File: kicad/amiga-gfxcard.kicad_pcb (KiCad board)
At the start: 2 copper layers, 127 x 59.1 mm, 34 parts, among them P1 ADDR1, P10 AUX1B, P11 AUX2A, P12 AUX2B, P2 ADDR2, P3 ADDR4, P4 DATA2, P5 ADDR3, P6 DATA1, P7 CTRL_OUT, P8 CONN_01X02, P9 AUX1A, U1 74LVC8T245, U2 74LVC8T245, U3 74LVC8T245, U4 74LVC8T245, U5 74LVC8T245, U6 74LVC8T245

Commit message: board v1.2 finished
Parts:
- removed P10: AUX1B, Pin_Headers:Pin_Header_Straight_1x08
- removed P11: AUX2A, Pin_Headers:Pin_Header_Straight_1x04
- removed P12: AUX2B, Pin_Headers:Pin_Header_Straight_1x04
- removed P7: CTRL_OUT, Pin_Headers:Pin_Header_Straight_1x04
- removed P9: AUX1A, Pin_Headers:Pin_Header_Straight_1x08
- added G***: LOGO, mnt:mnt, F.Cu at (203.2, 49.7)
- added P13: X1, Pin_Headers:Pin_Header_Straight_1x08, F.Cu at (137.8, 50.2)
- added P14: X2, Pin_Headers:Pin_Header_Straight_1x08, F.Cu at (137.8, 47.6)
- added P16: D1, Pin_Headers:Pin_Header_Straight_1x03, F.Cu at (130.3, 94.6)
- moved C1 45.7 mm to (102.5, 104.0)
- moved C10 45.7 mm to (121.4, 113.0)
- moved C11 45.7 mm to (142.2, 103.9)
- moved C12 45.7 mm to (184.2, 114.2)
- moved C2 45.7 mm to (162.0, 113.0)
- moved C3 45.7 mm to (152.1, 103.9)
- moved C4 45.7 mm to (102.5, 113.0)
- moved C5 45.7 mm to (161.9, 103.9)
- moved C6 45.7 mm to (152.1, 112.8)
- moved C7 45.7 mm to (184.2, 104.0)
- moved C8 45.7 mm to (142.2, 112.8)
- moved C9 45.7 mm to (121.4, 104.0)
- moved P1 45.7 mm to (137.9, 92.1)
- moved P2 45.7 mm to (137.9, 94.6)
- moved P3 45.7 mm to (158.2, 94.6)
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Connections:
- CON-Z21 pad 10: Net-(CON-Z21-Pad10) -> (no net)
- CON-Z21 pad 14: Net-(CON-Z21-Pad14) -> (no net)
- CON-Z21 pad 15: Net-(CON-Z21-Pad15) -> (no net)
- CON-Z21 pad 16: Net-(CON-Z21-Pad16) -> (no net)
- CON-Z21 pad 17: Net-(CON-Z21-Pad17) -> (no net)
- CON-Z21 pad 18: Net-(CON-Z21-Pad18) -> (no net)
- CON-Z21 pad 19: Net-(CON-Z21-Pad19) -> (no net)
- CON-Z21 pad 20: Net-(CON-Z21-Pad20) -> (no net)
- CON-Z21 pad 22: Net-(CON-Z21-Pad22) -> (no net)
- CON-Z21 pad 31: Net-(CON-Z21-Pad31) -> (no net)
- CON-Z21 pad 33: Net-(CON-Z21-Pad33) -> (no net)
- CON-Z21 pad 35: Net-(CON-Z21-Pad35) -> (no net)
- CON-Z21 pad 40: Net-(CON-Z21-Pad40) -> (no net)
- CON-Z21 pad 42: Net-(CON-Z21-Pad42) -> (no net)
- CON-Z21 pad 44: Net-(CON-Z21-Pad44) -> (no net)
- CON-Z21 pad 48: Net-(CON-Z21-Pad48) -> (no net)
- CON-Z21 pad 50: Net-(CON-Z21-Pad50) -> (no net)
- CON-Z21 pad 51: Net-(CON-Z21-Pad51) -> (no net)
- CON-Z21 pad 55: Net-(CON-Z21-Pad55) -> (no net)
- CON-Z21 pad 60: Net-(CON-Z21-Pad60) -> (no net)
- CON-Z21 pad 62: Net-(CON-Z21-Pad62) -> (no net)
- CON-Z21 pad 64: Net-(CON-Z21-Pad64) -> (no net)
- CON-Z21 pad 66: Net-(CON-Z21-Pad66) -> (no net)
- CON-Z21 pad 7: Net-(CON-Z21-Pad7) -> (no net)
- CON-Z21 pad 8: Net-(CON-Z21-Pad8) -> (no net)
- CON-Z21 pad 91: Net-(CON-Z21-Pad91) -> (no net)
- CON-Z21 pad 94: Net-(CON-Z21-Pad94) -> (no net)
- CON-Z21 pad 95: Net-(CON-Z21-Pad95) -> (no net)
- CON-Z21 pad 96: Net-(CON-Z21-Pad96) -> (no net)
- CON-Z21 pad 97: Net-(CON-Z21-Pad97) -> (no net)
- CON-Z21 pad 98: Net-(CON-Z21-Pad98) -> (no net)
- P1 pad 1: Net-(P1-Pad1) -> (no net)
- P1 pad 5: Net-(P1-Pad5) -> (no net)
- P2 pad 1: Net-(P2-Pad1) -> (no net)
- P2 pad 5: Net-(P2-Pad5) -> (no net)
- P3 pad 1: Net-(P3-Pad1) -> (no net)
- P3 pad 5: Net-(P3-Pad5) -> (no net)
- P4 pad 1: Net-(P4-Pad1) -> (no net)
- P4 pad 5: Net-(P4-Pad5) -> (no net)
- P5 pad 1: Net-(P5-Pad1) -> (no net)
- P5 pad 5: Net-(P5-Pad5) -> (no net)
- P6 pad 1: Net-(P6-Pad1) -> (no net)
- P6 pad 5: Net-(P6-Pad5) -> (no net)
- R3 pad 1: Net-(P7-Pad4) -> Net-(P16-Pad3)
- U1 pad 17: Net-(P1-Pad5) -> Net-(P13-Pad8)
- U1 pad 21: Net-(P1-Pad1) -> Net-(P13-Pad7)
- U2 pad 17: Net-(P2-Pad5) -> Net-(P14-Pad8)
- U2 pad 2: Net-(P7-Pad4) -> +5V
- U2 pad 21: Net-(P2-Pad1) -> Net-(P14-Pad7)
- U3 pad 17: Net-(P3-Pad5) -> Net-(P14-Pad3)
- U3 pad 21: Net-(P3-Pad1) -> Net-(P14-Pad2)
- U4 pad 17: Net-(P4-Pad5) -> Net-(P13-Pad6)
- U4 pad 2: Net-(P7-Pad4) -> Net-(P16-Pad3)
- U4 pad 21: Net-(P4-Pad1) -> Net-(P13-Pad4)
- U5 pad 17: Net-(P5-Pad5) -> Net-(P14-Pad6)
- U5 pad 21: Net-(P5-Pad1) -> Net-(P14-Pad4)
- U6 pad 17: Net-(P6-Pad5) -> Net-(P13-Pad3)
- U6 pad 2: +5V -> Net-(P16-Pad3)
- U6 pad 21: Net-(P6-Pad1) -> Net-(P13-Pad2)
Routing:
- net Net-(P14-Pad4): track 0.00 -> 85.8 mm, vias 0 -> 1
- net Net-(P13-Pad7): track 0.00 -> 83.7 mm, vias 0 -> 4
- net Net-(P13-Pad4): track 0.00 -> 81.2 mm, vias 0 -> 1
- net Net-(P13-Pad6): track 0.00 -> 80.9 mm, vias 0 -> 1
- net Net-(P14-Pad6): track 0.00 -> 80.7 mm, vias 0 -> 1
- net Net-(P13-Pad8): track 0.00 -> 79.7 mm, vias 0 -> 3
- net Net-(P16-Pad3): track 0.00 -> 72.8 mm, vias 0 -> 2
- net Net-(P14-Pad7): track 0.00 -> 72.5 mm, vias 0 -> 1
- net Net-(P7-Pad4): track 70.5 -> 0.00 mm, vias 2 -> 0
- net Net-(P13-Pad2): track 0.00 -> 68.2 mm, vias 0 -> 3
- net Net-(P14-Pad3): track 0.00 -> 68.0 mm, vias 0 -> 3
- net Net-(P14-Pad2): track 0.00 -> 68.0 mm
- net Net-(P13-Pad3): track 0.00 -> 62.0 mm, vias 0 -> 1
- net Net-(P14-Pad8): track 0.00 -> 61.1 mm, vias 0 -> 1
- net Net-(P4-Pad8): track 12.8 -> 71.2 mm, vias 0 -> 1
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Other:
- board size 127 x 59.1 mm -> 127 x 96 mm
- board text added: "2016-02-21 Amiga 2000 FPGA Carrier v1.2 mntmn.com"
- board text added: "A"
- board text added: "A4-12"
- board text added: "B"
- board text added: "D"
- board text added: "D0-2 D11-15"
- board text added: "D3-10"
- board text added: "E"
- board text added: "F"
- board text added: "U1"
- board text added: "U2"
- board text added: "U3"
- board text added: "U4"
- board text added: "U5"
- board text added: "U6"

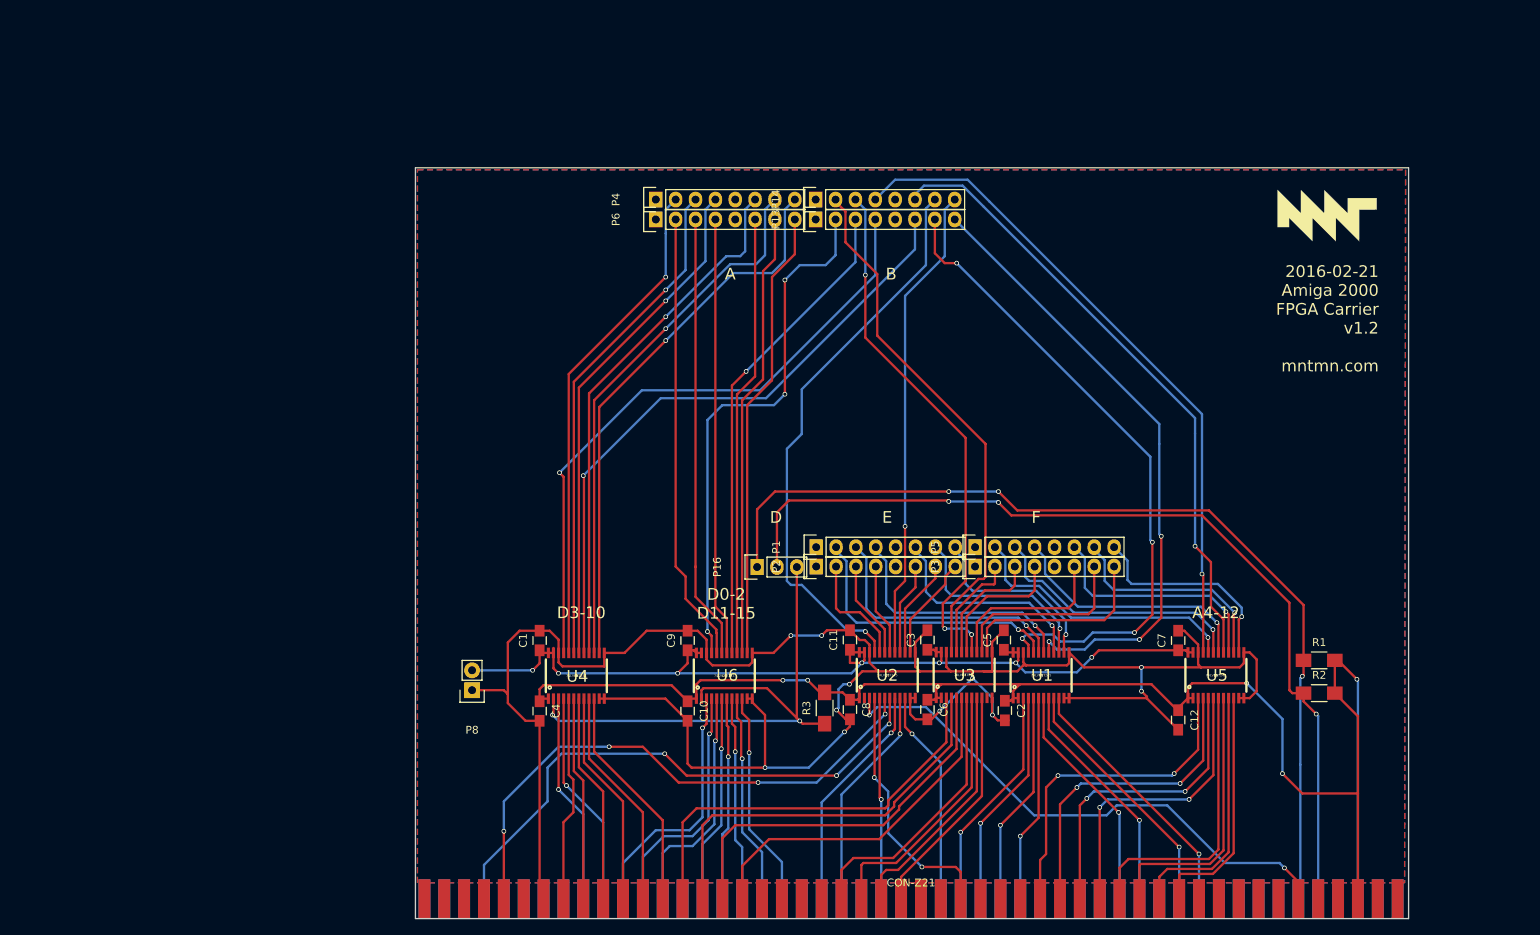
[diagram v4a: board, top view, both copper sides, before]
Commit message: Version 2, new board, minispartan 6+, working DVI/HDMI output
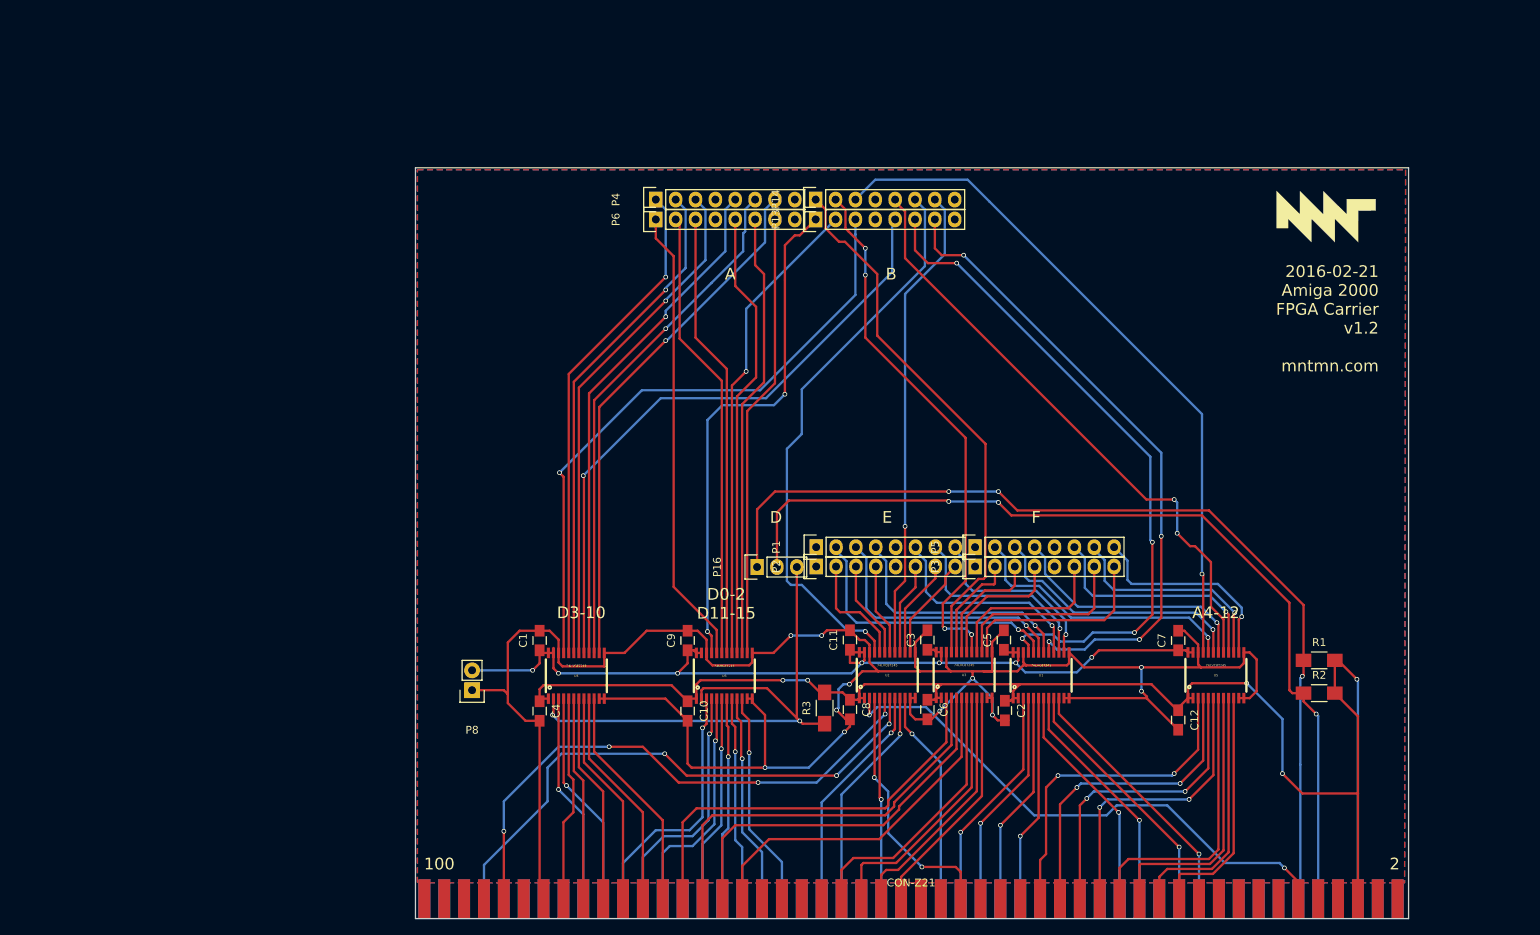
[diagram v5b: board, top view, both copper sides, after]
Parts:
- moved G*** 0.18 mm to (203.1, 49.8)
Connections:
- CON-Z21 pad 10: (no net) -> Net-(CON-Z21-Pad10)
- CON-Z21 pad 14: (no net) -> Net-(CON-Z21-Pad14)
- CON-Z21 pad 15: (no net) -> Net-(CON-Z21-Pad15)
- CON-Z21 pad 16: (no net) -> Net-(CON-Z21-Pad16)
- CON-Z21 pad 17: (no net) -> Net-(CON-Z21-Pad17)
- CON-Z21 pad 18: (no net) -> Net-(CON-Z21-Pad18)
- CON-Z21 pad 19: (no net) -> Net-(CON-Z21-Pad19)
- CON-Z21 pad 20: (no net) -> Net-(CON-Z21-Pad20)
- CON-Z21 pad 22: (no net) -> Net-(CON-Z21-Pad22)
- CON-Z21 pad 31: (no net) -> Net-(CON-Z21-Pad31)
- CON-Z21 pad 33: (no net) -> Net-(CON-Z21-Pad33)
- CON-Z21 pad 35: (no net) -> Net-(CON-Z21-Pad35)
- CON-Z21 pad 40: (no net) -> Net-(CON-Z21-Pad40)
- CON-Z21 pad 42: (no net) -> Net-(CON-Z21-Pad42)
- CON-Z21 pad 44: (no net) -> Net-(CON-Z21-Pad44)
- CON-Z21 pad 48: (no net) -> Net-(CON-Z21-Pad48)
- CON-Z21 pad 50: (no net) -> Net-(CON-Z21-Pad50)
- CON-Z21 pad 51: (no net) -> Net-(CON-Z21-Pad51)
- CON-Z21 pad 55: (no net) -> Net-(CON-Z21-Pad55)
- CON-Z21 pad 60: (no net) -> Net-(CON-Z21-Pad60)
- CON-Z21 pad 62: (no net) -> Net-(CON-Z21-Pad62)
- CON-Z21 pad 64: (no net) -> Net-(CON-Z21-Pad64)
- CON-Z21 pad 66: (no net) -> Net-(CON-Z21-Pad66)
- CON-Z21 pad 7: (no net) -> Net-(CON-Z21-Pad7)
- CON-Z21 pad 8: (no net) -> Net-(CON-Z21-Pad8)
- CON-Z21 pad 91: (no net) -> Net-(CON-Z21-Pad91)
- CON-Z21 pad 94: (no net) -> Net-(CON-Z21-Pad94)
- CON-Z21 pad 95: (no net) -> Net-(CON-Z21-Pad95)
- CON-Z21 pad 96: (no net) -> Net-(CON-Z21-Pad96)
- CON-Z21 pad 97: (no net) -> Net-(CON-Z21-Pad97)
- CON-Z21 pad 98: (no net) -> Net-(CON-Z21-Pad98)
- P1 pad 1: (no net) -> Net-(P1-Pad1)
- P1 pad 5: (no net) -> Net-(P1-Pad5)
- P13 pad 1: (no net) -> Net-(P13-Pad1)
- P13 pad 5: (no net) -> Net-(P13-Pad5)
- P14 pad 1: (no net) -> Net-(P14-Pad1)
- P14 pad 5: (no net) -> Net-(P14-Pad5)
- P2 pad 1: (no net) -> Net-(P2-Pad1)
- P2 pad 5: (no net) -> Net-(P2-Pad5)
- P3 pad 1: (no net) -> Net-(P3-Pad1)
- P3 pad 5: (no net) -> Net-(P3-Pad5)
- P4 pad 1: (no net) -> Net-(P4-Pad1)
- P4 pad 5: (no net) -> Net-(P4-Pad5)
- P5 pad 1: (no net) -> Net-(P5-Pad1)
- P5 pad 5: (no net) -> Net-(P5-Pad5)
- P6 pad 1: (no net) -> Net-(P6-Pad1)
- P6 pad 5: (no net) -> Net-(P6-Pad5)
- U1 pad 17: Net-(P13-Pad8) -> Net-(P13-Pad7)
- U1 pad 21: Net-(P13-Pad7) -> Net-(P13-Pad6)
- U2 pad 17: Net-(P14-Pad8) -> Net-(P14-Pad7)
- U2 pad 21: Net-(P14-Pad7) -> Net-(P14-Pad6)
- U3 pad 17: Net-(P14-Pad3) -> Net-(P14-Pad2)
- U3 pad 21: Net-(P14-Pad2) -> Net-(P14-Pad1)
- U4 pad 14: Net-(P4-Pad8) -> Net-(P4-Pad7)
- U4 pad 15: Net-(P4-Pad7) -> Net-(P4-Pad6)
- U4 pad 16: Net-(P4-Pad6) -> Net-(P4-Pad5)
- U4 pad 17: Net-(P13-Pad6) -> Net-(P13-Pad5)
- U4 pad 18: Net-(P4-Pad4) -> Net-(P4-Pad3)
- U4 pad 19: Net-(P4-Pad3) -> Net-(P4-Pad2)
- U4 pad 20: Net-(P4-Pad2) -> Net-(P4-Pad1)
- U4 pad 21: Net-(P13-Pad4) -> Net-(P13-Pad3)
- U5 pad 17: Net-(P14-Pad6) -> Net-(P14-Pad5)
- U5 pad 21: Net-(P14-Pad4) -> Net-(P14-Pad3)
- U6 pad 14: Net-(P6-Pad8) -> Net-(P6-Pad7)
- U6 pad 15: Net-(P6-Pad7) -> Net-(P6-Pad6)
- U6 pad 16: Net-(P6-Pad6) -> Net-(P6-Pad5)
- U6 pad 17: Net-(P13-Pad3) -> Net-(P13-Pad2)
- U6 pad 18: Net-(P6-Pad4) -> Net-(P6-Pad3)
- U6 pad 19: Net-(P6-Pad3) -> Net-(P6-Pad2)
- U6 pad 20: Net-(P6-Pad2) -> Net-(P6-Pad1)
- U6 pad 21: Net-(P13-Pad2) -> Net-(P13-Pad1)
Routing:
- net Net-(P14-Pad4): track 85.8 -> 0.00 mm, vias 1 -> 0
- net Net-(P13-Pad4): track 81.2 -> 0.00 mm, vias 1 -> 0
- net Net-(P13-Pad5): track 0.00 -> 79.9 mm, vias 0 -> 1
- net Net-(P13-Pad8): track 79.7 -> 0.00 mm, vias 3 -> 0
- net Net-(P14-Pad5): track 0.00 -> 77.8 mm, vias 0 -> 2
- net Net-(P4-Pad8): track 71.2 -> 0.00 mm, vias 1 -> 0
- net Net-(P14-Pad1): track 0.00 -> 69.5 mm
- net Net-(P4-Pad5): track 0.00 -> 65.7 mm, vias 0 -> 1
- net Net-(P13-Pad1): track 0.00 -> 65.6 mm, vias 0 -> 2
- net Net-(P4-Pad4): track 65.2 -> 0.00 mm, vias 1 -> 0
- net Net-(P4-Pad1): track 0.00 -> 63.6 mm, vias 0 -> 1
- net Net-(P14-Pad8): track 61.1 -> 0.00 mm, vias 1 -> 0
- net Net-(P6-Pad1): track 0.00 -> 58.7 mm
- net Net-(P6-Pad8): track 58.0 -> 0.00 mm
- net Net-(P6-Pad5): track 0.00 -> 57.5 mm
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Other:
- board text added: "100"
- board text added: "2"
- board text removed: "U1"
- board text removed: "U2"
- board text removed: "U3"
- board text removed: "U4"
- board text removed: "U5"
- board text removed: "U6"
